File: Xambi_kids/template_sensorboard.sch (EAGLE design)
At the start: 6 parts

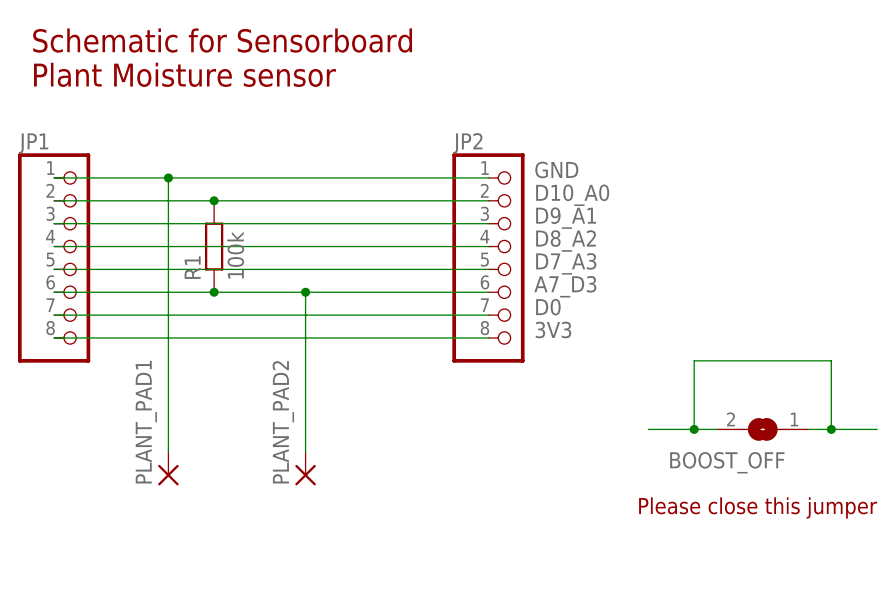
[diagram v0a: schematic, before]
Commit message: change template for sensor images
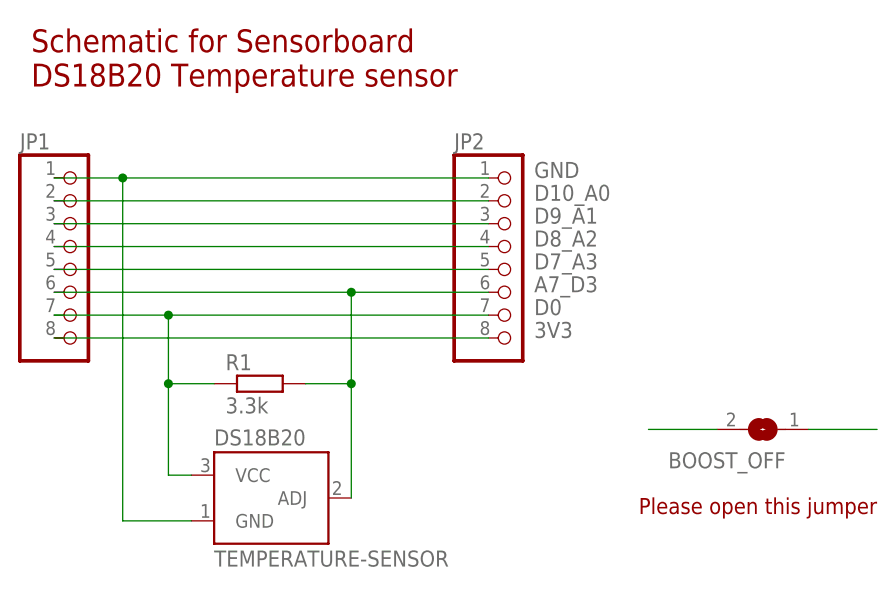
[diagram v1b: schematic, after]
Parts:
- removed PLANT_PAD1, PLANT_PAD2: (no value), wirepad:2,15/1,0
- added DS18B20: TEMPERATURE-SENSOR, SparkFun-Sensors:TEMPERATURE-SENSOR
- R1: value 100k -> 3.3k; device rcl:R-EU_0207/12 -> rcl:R-EU_0207/15
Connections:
- new net N$1: BOOST_OFF.2
- net A7_D3: now also DS18B20.ADJ, R1.2; no longer PLANT_PAD2.P, R1.1
- net D0: now also DS18B20.VCC, R1.1
- net D10_A0: no longer R1.2
- net GND: now also DS18B20.GND; no longer PLANT_PAD1.P
- net N$2: no longer BOOST_OFF.2
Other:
- note added: "Please open this jumper"
- note added: "Schematic for Sensorboard DS18B20 Temperature sensor"
- note removed: "Please close this jumper"
- note removed: "Schematic for Sensorboard Plant Moisture sensor"
- moved on the sheet: R1
